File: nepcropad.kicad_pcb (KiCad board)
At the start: 2 copper layers, 99.2 x 58.7 mm, 34 parts, among them SW1 SW_Push, U1 ATmega32U4-A, Y1 16MHz

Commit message: Finished routing
I think atleast.
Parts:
- moved D1 17.5 mm to (158.0, 71.4)
- moved D2 17.5 mm to (177.0, 71.5)
- moved D3 17.5 mm to (196.1, 71.4)
- moved D4 17.5 mm to (158.0, 90.5)
- moved D5 17.5 mm to (177.0, 90.5)
- moved D6 17.5 mm to (196.1, 90.5)
- moved D7 17.5 mm to (158.0, 109.5)
- moved D8 17.5 mm to (177.0, 109.5)
- moved D9 17.5 mm to (196.1, 109.5)
- moved MX1 17.5 mm to (150.0, 71.4)
- moved MX2 17.5 mm to (169.1, 71.4)
- moved MX3 17.5 mm to (188.1, 71.4)
- moved MX4 17.5 mm to (150.0, 90.5)
- moved MX5 17.5 mm to (169.1, 90.5)
- moved MX6 17.5 mm to (188.1, 90.5)
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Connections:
- U1 pad 26: unconnected-(U1-Pad26) -> ROW0
- U1 pad 27: unconnected-(U1-Pad27) -> ROW1
- U1 pad 28: unconnected-(U1-Pad28) -> COL2
- U1 pad 29: unconnected-(U1-Pad29) -> COL1
- U1 pad 30: unconnected-(U1-Pad30) -> COL0
- U1 pad 31: unconnected-(U1-Pad31) -> ROW2
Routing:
- net COL2: track 38.1 -> 112.1 mm
- net COL1: track 38.1 -> 92.7 mm
- net ROW2: track 39.3 -> 88.3 mm
- net ROW0: track 39.2 -> 87.2 mm
- net ROW1: track 39.3 -> 81.7 mm
- net COL0: track 38.1 -> 73.3 mm
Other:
- board size 99.2 x 58.7 mm -> 116.7 x 58.7 mm

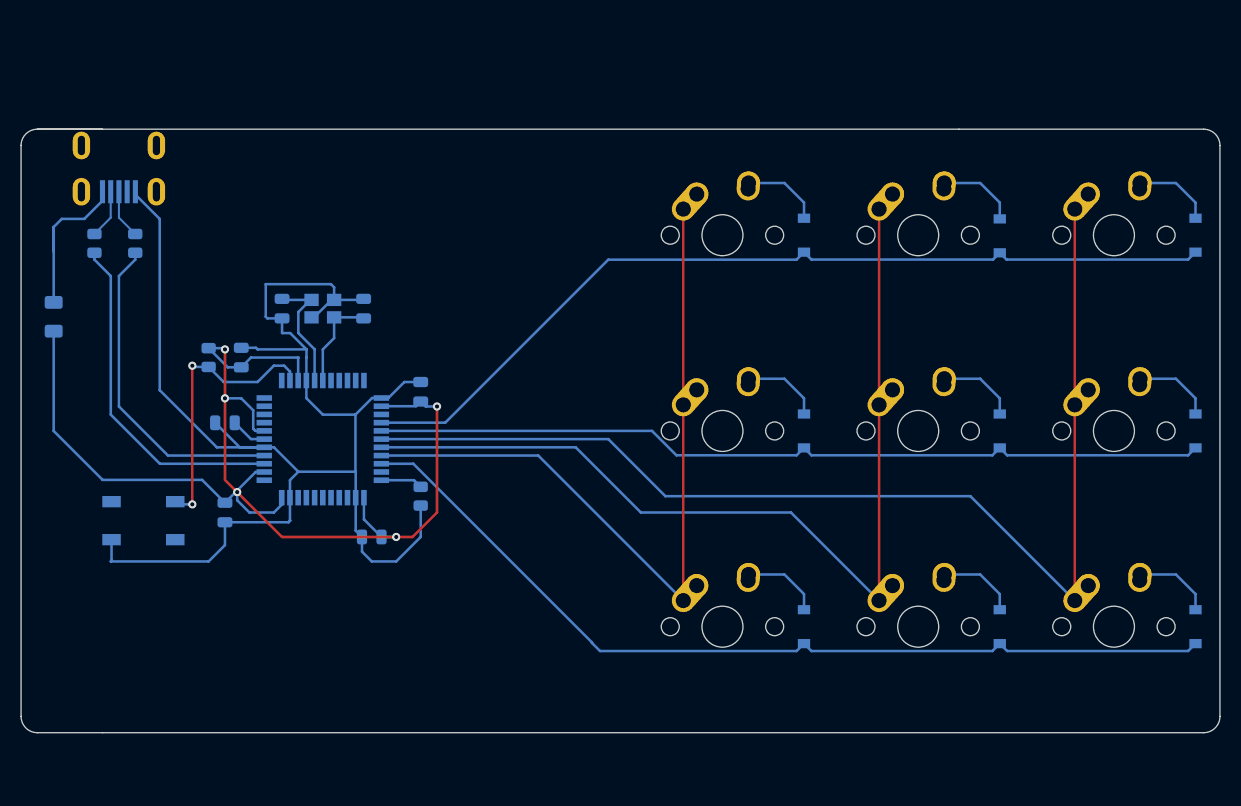
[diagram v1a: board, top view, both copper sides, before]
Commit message: Rerouted matrix
moved closer to soc for more cost efficiency probably.
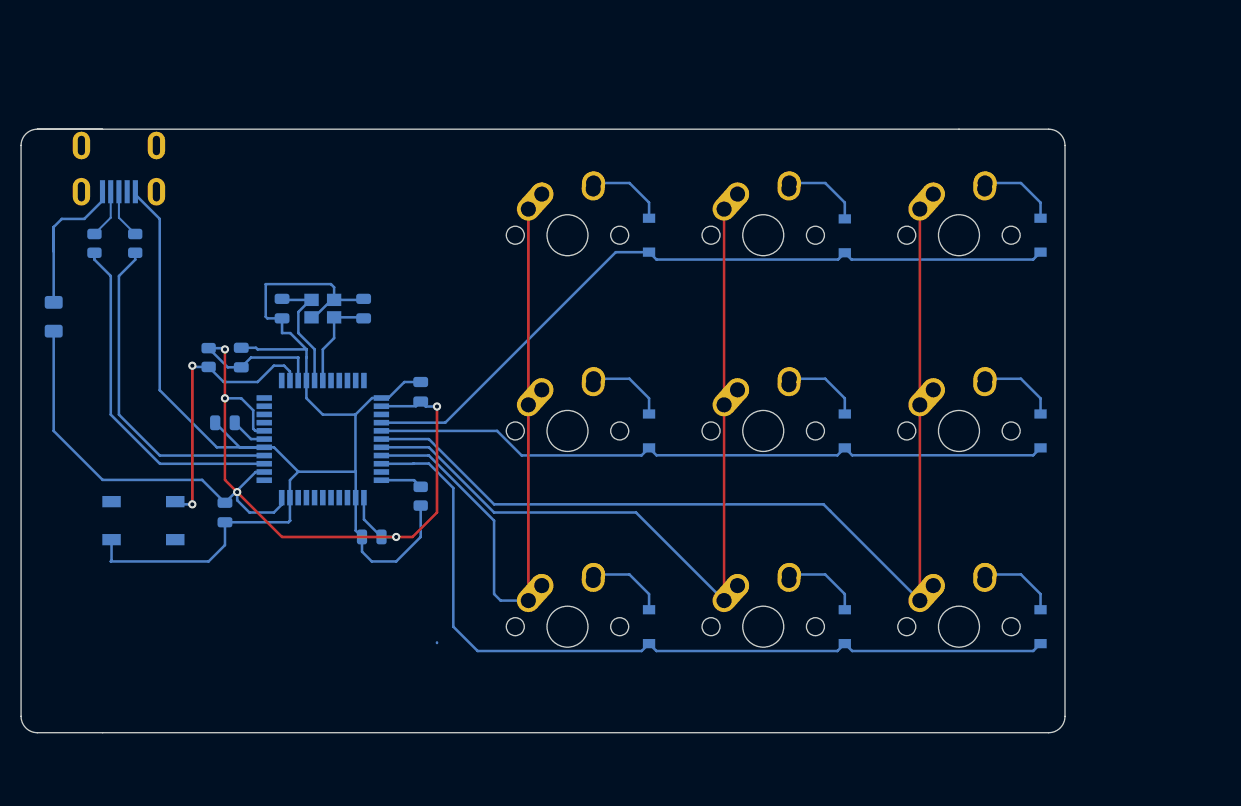
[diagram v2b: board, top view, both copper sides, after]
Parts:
- moved D1 15.1 mm to (142.9, 71.4)
- moved D3 15.1 mm to (181.0, 71.4)
- moved D4 15.1 mm to (142.9, 90.5)
- moved D6 15.1 mm to (181.0, 90.5)
- moved D7 15.1 mm to (142.9, 109.5)
- moved D9 15.1 mm to (181.0, 109.5)
- moved MX1 15.1 mm to (134.9, 71.4)
- moved MX3 15.1 mm to (173.0, 71.4)
- moved MX4 15.1 mm to (134.9, 90.5)
- moved MX6 15.1 mm to (173.0, 90.5)
- moved MX7 15.1 mm to (134.9, 109.5)
- moved MX9 15.1 mm to (173.0, 109.5)
- moved D2 15.1 mm to (161.9, 71.5)
- moved D5 15.1 mm to (161.9, 90.5)
- moved D8 15.1 mm to (161.9, 109.5)
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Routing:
- net COL2: track 112.1 -> 97.0 mm
- net COL1: track 92.7 -> 77.6 mm
- net ROW0: track 87.2 -> 72.2 mm
- net ROW1: track 81.7 -> 66.6 mm
- net COL0: track 73.3 -> 62.4 mm
- net ROW2: track 88.3 -> 81.2 mm
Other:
- board size 116.7 x 58.7 mm -> 101.6 x 58.7 mm

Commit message: minimize pcb
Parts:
- removed USB1: Molex-0548190589, random-keyboard-parts:Molex-0548190589
- added J1: USB_C_Receptacle_USB2.0, usbc:USB_C_GCT_USB4085, F.Cu at (144.8, 55.1)
- added R5: 5.1k, resistor:R_0805_2012Metric, B.Cu at (148.0, 62.9)
- added R6: 5.1k, resistor:R_0805_2012Metric, F.Cu at (137.8, 59.1)
- C4, C5, C6, C7: moved to F.Cu
- moved SW1 92.2 mm to (176.8, 59.4)
- moved F1 73.3 mm to (154.9, 57.8), turned to 0 degrees
- moved C2 71.3 mm to (178.4, 74.7), turned to 180 degrees
- moved R1 71.2 mm to (167.6, 61.0), turned to 0 degrees
- moved C7 68.3 mm to (158.8, 61.0)
- moved Y1 67.4 mm to (178.5, 77.7)
- moved C1 63.4 mm to (178.5, 81.0), turned to 0 degrees
- moved C3 61.3 mm to (159.3, 68.8), turned to 135 degrees
- moved C6 56.7 mm to (156.2, 61.0), turned to -90 degrees
- moved R3 54.6 mm to (143.5, 71.1)
- moved U1 53.9 mm to (163.5, 78.7), turned to -45 degrees
- moved R2 53.2 mm to (146.1, 71.1)
- moved C4 52.9 mm to (151.1, 61.0), turned to -90 degrees
- moved R4 43.3 mm to (163.3, 89.4), turned to 0 degrees
- moved C5 41.9 mm to (153.7, 61.0), turned to -90 degrees
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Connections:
- U1 pad 29: COL1 -> ROW2
- U1 pad 30: COL0 -> COL1
- U1 pad 31: ROW2 -> COL0
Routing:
- net COL2: track 97.0 -> 43.1 mm
- net +5V: track 119.6 -> 84.8 mm, vias 5 -> 4
- net COL0: track 62.4 -> 85.7 mm
- net Net-(R2-Pad2): track 32.2 -> 13.9 mm
- net Net-(R3-Pad2): track 33.3 -> 16.1 mm
- net GND: track 147.2 -> 132.9 mm, vias 0 -> 3
- net Net-(C1-Pad2): track 9.52 -> 22.0 mm
- net ROW1: track 66.6 -> 54.4 mm
- net ROW2: track 81.2 -> 71.2 mm, vias 0 -> 2
- net Net-(J1-PadB5): track 0.00 -> 7.41 mm
- net COL1: track 77.6 -> 70.5 mm
- net D+: track 4.77 -> 11.1 mm
- net D-: track 4.77 -> 11.1 mm
- net Net-(C3-Pad1): track 3.53 -> 7.69 mm
- net Net-(D1-Pad2): track 7.71 -> 3.96 mm
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- added copper zone on F.Cu, net GND
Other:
- board size 101.6 x 58.7 mm -> 58.7 x 65.2 mm

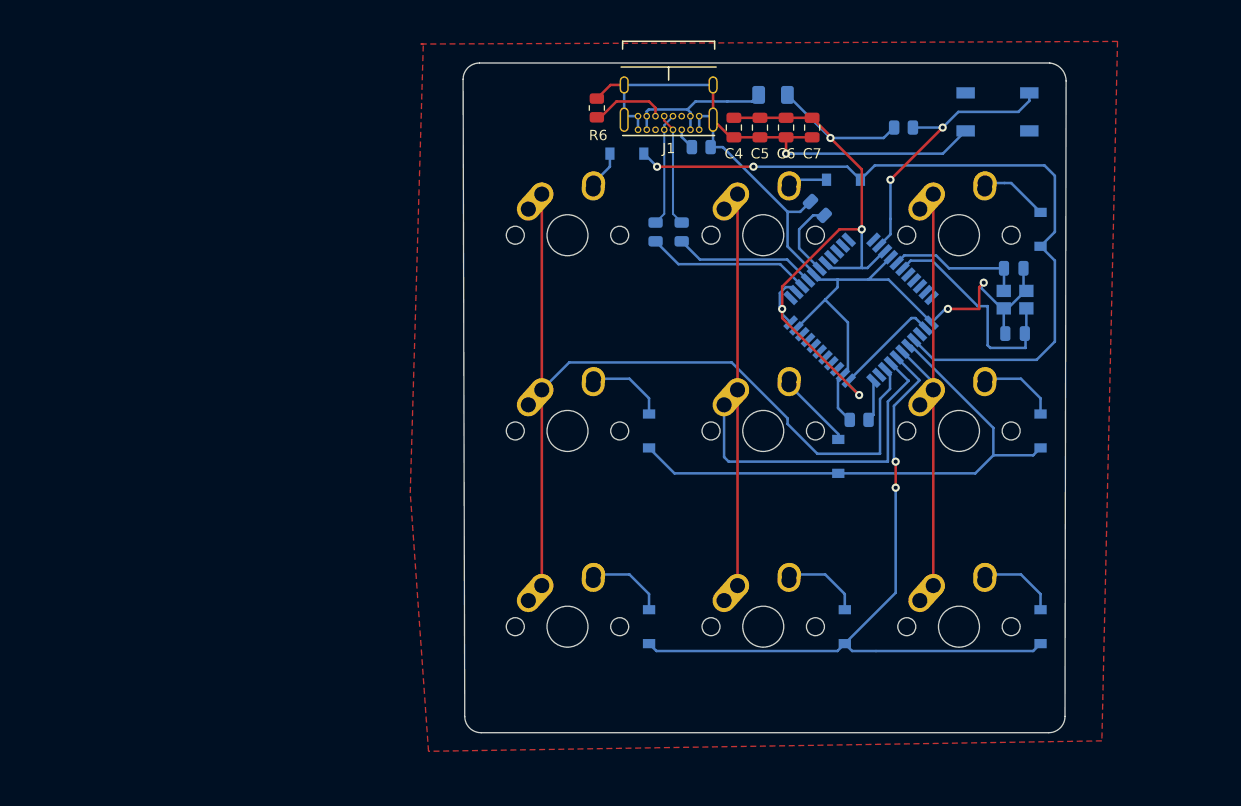
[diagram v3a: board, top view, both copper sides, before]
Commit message: move SMC's to same side to cut costs
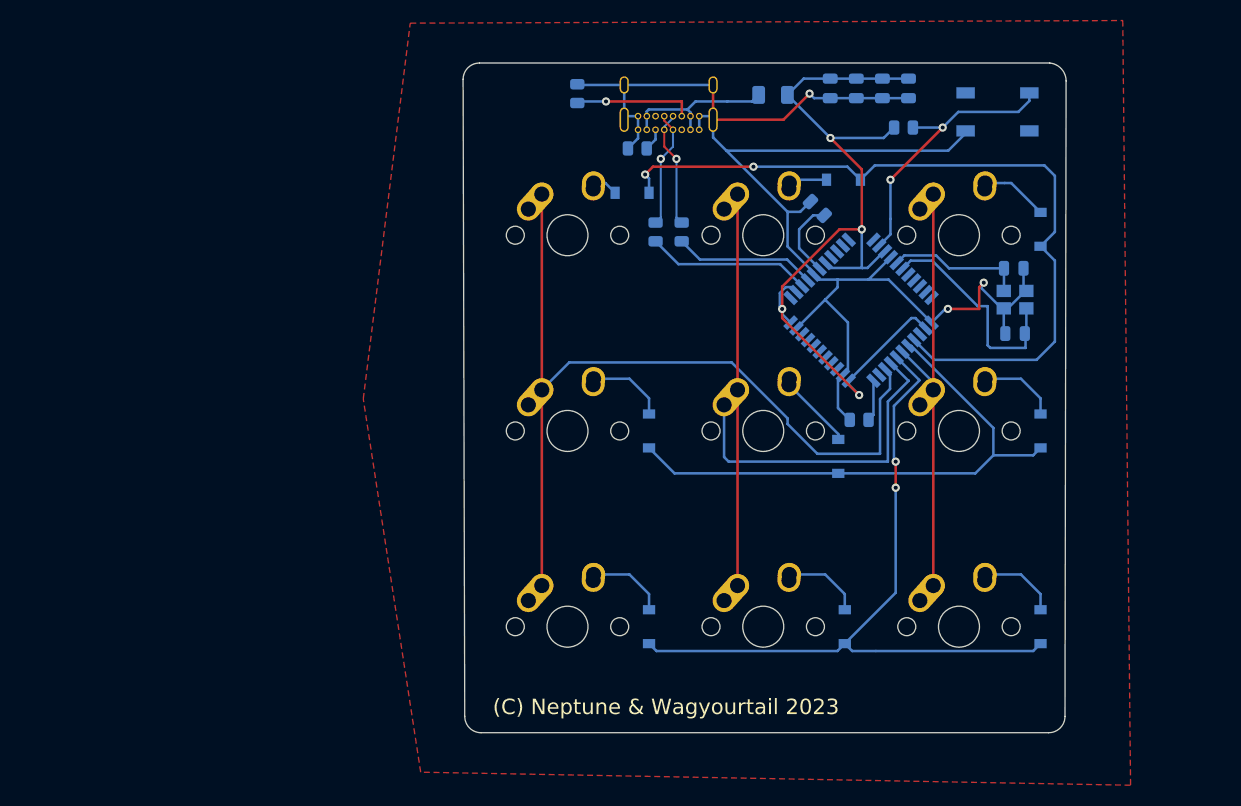
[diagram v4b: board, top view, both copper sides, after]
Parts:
- C4, C5, C6, C7, J1, R6: moved to B.Cu
- moved C4 17.4 mm to (168.1, 57.1)
- moved C5 12.5 mm to (165.6, 57.1)
- moved C6 7.83 mm to (163.0, 57.1)
- moved R5 6.22 mm to (141.7, 63.0), turned to 180 degrees
- moved C7 4.20 mm to (160.5, 57.1)
- moved D1 3.84 mm to (141.2, 67.3)
- moved R6 2.36 mm to (135.9, 57.7)
- turned J1 to 0 degrees
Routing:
- net GND: track 132.9 -> 150.1 mm
- net Net-(J1-PadB5): track 7.41 -> 11.9 mm, vias 0 -> 1
- net +5V: track 84.8 -> 87.1 mm
- net ROW0: track 74.6 -> 76.2 mm
- net Net-(D1-Pad2): track 3.96 -> 2.49 mm
- net D-: track 11.1 -> 11.4 mm, vias 0 -> 1
- net D+: track 11.1 -> 11.4 mm, vias 0 -> 1
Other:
- board text added: "(C) Neptune & Wagyourtail 2023"

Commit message: cleanup
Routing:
- net COL0: track 85.7 -> 85.0 mm
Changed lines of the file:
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@@
   (segment (start 160.011508 77.715508) (end 157.21925 80.507767) (width 0.25) (layer "B.Cu") (net 1))
   (segment (start 179.319 76.581) (end 179.596 76.858) (width 0.25) (layer "B.Cu") (net 1))
-  (segment (start 168.12569 58.1) (end 168.43569 58.1) (width 0.25) (layer "B.Cu") (net 1))
   (segment (start 141.805 61.175) (end 141.805 62.0065) (width 0.25) (layer "B.Cu") (net 1))
   (segment (start 161.222725 75.759275) (end 164.230483 75.759275) (width 0.25) (layer "B.Cu") (net 1))
@@
   (segment (start 158.840249 69.505751) (end 159.929751 69.505751) (width 0.25) (layer "B.Cu") (net 4))
   (segment (start 160.528 61.976) (end 163.576 65.024) (width 0.25) (layer "F.Cu") (net 5))
-  (segment (start 160.528 61.976) (end 160.528 61.788) (width 0.25) (layer "F.Cu") (net 5))
   (segment (start 163.576 70.866) (end 161.406769 70.866) (width 0.25) (layer "F.Cu") (net 5))
   (segment (start 155.829 79.502) (end 155.829 78.613) (width 0.25) (layer "F.Cu") (net 5))
@@
   (segment (start 165.354 92.71) (end 159.258 92.71) (width 0.25) (layer "B.Cu") (net 19))
   (segment (start 156.356401 89.262861) (end 150.91354 83.82) (width 0.25) (layer "B.Cu") (net 19))
-  (segment (start 165.845952 84.467565) (end 166.37 84.991613) (width 0.25) (layer "B.Cu") (net 19))
   (segment (start 165.354 87.376) (end 165.354 92.71) (width 0.25) (layer "B.Cu") (net 19))
   (segment (start 166.330051 84.951664) (end 166.330051 86.399949) (width 0.25) (layer "B.Cu") (net 19))
@@
   (segment (start 166.411638 83.90188) (end 168.107758 85.598) (width 0.25) (layer "B.Cu") (net 20))
   (segment (start 166.116 87.63) (end 166.116 93.472) (width 0.25) (layer "B.Cu") (net 20))
-  (segment (start 168.107758 85.598) (end 168.148 85.598) (width 0.25) (layer "B.Cu") (net 20))
   (segment (start 150.1775 93.0275) (end 150.1775 87.9475) (width 0.25) (layer "B.Cu") (net 20))
   (segment (start 168.148 85.598) (end 166.116 87.63) (width 0.25) (layer "B.Cu") (net 20))
@@
   (segment (start 146.06 58.43) (end 146.05 58.42) (width 0.25) (layer "F.Cu") (net 49))
   (via (at 138.684 58.42) (size 0.8) (drill 0.4) (layers "F.Cu" "B.Cu") (net 49))
-  (segment (start 138.5335 58.5705) (end 138.684 58.42) (width 0.25) (layer "B.Cu") (net 49))
   (segment (start 136.0405 58.42) (end 135.89 58.5705) (width 0.25) (layer "B.Cu") (net 49))
   (segment (start 138.684 58.42) (end 136.0405 58.42) (width 0.25) (layer "B.Cu") (net 49))

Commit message: move some caps and the timer
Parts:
- moved C4 30.7 mm to (147.6, 80.0)
- moved C5 27.9 mm to (149.6, 80.0)
- moved C6 25.5 mm to (151.6, 80.0)
- moved C7 23.9 mm to (153.7, 80.0)
- moved Y1 3.57 mm to (175.3, 76.2), turned to 135 degrees
- moved C1 2.70 mm to (177.5, 78.5), turned to -135 degrees
- moved C2 0.96 mm to (177.5, 74.2), turned to 135 degrees
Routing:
- net Net-(C1-Pad2): track 22.0 -> 11.9 mm
- net GND: track 149.8 -> 141.1 mm, vias 3 -> 0
- net +5V: track 86.9 -> 82.9 mm
- net Net-(C2-Pad2): track 13.5 -> 11.3 mm

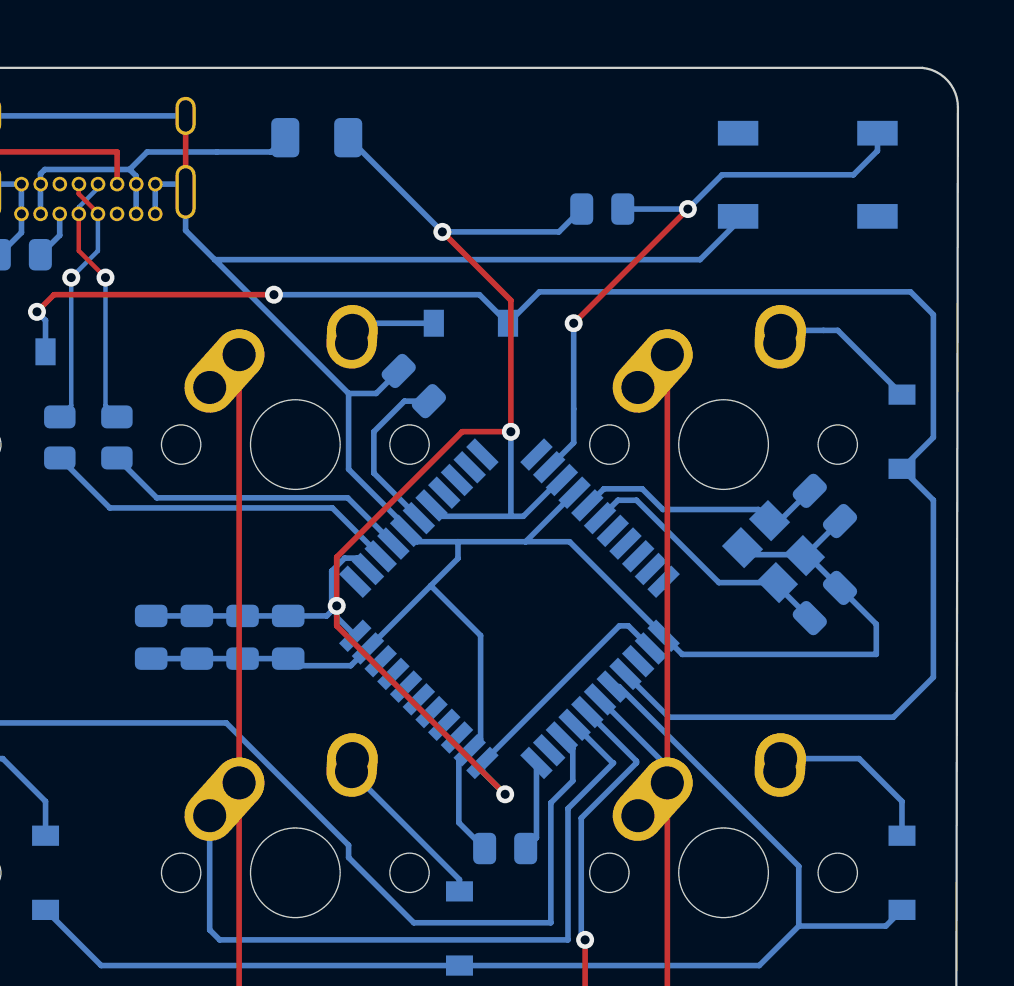
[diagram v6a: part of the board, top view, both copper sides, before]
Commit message: update cap positions
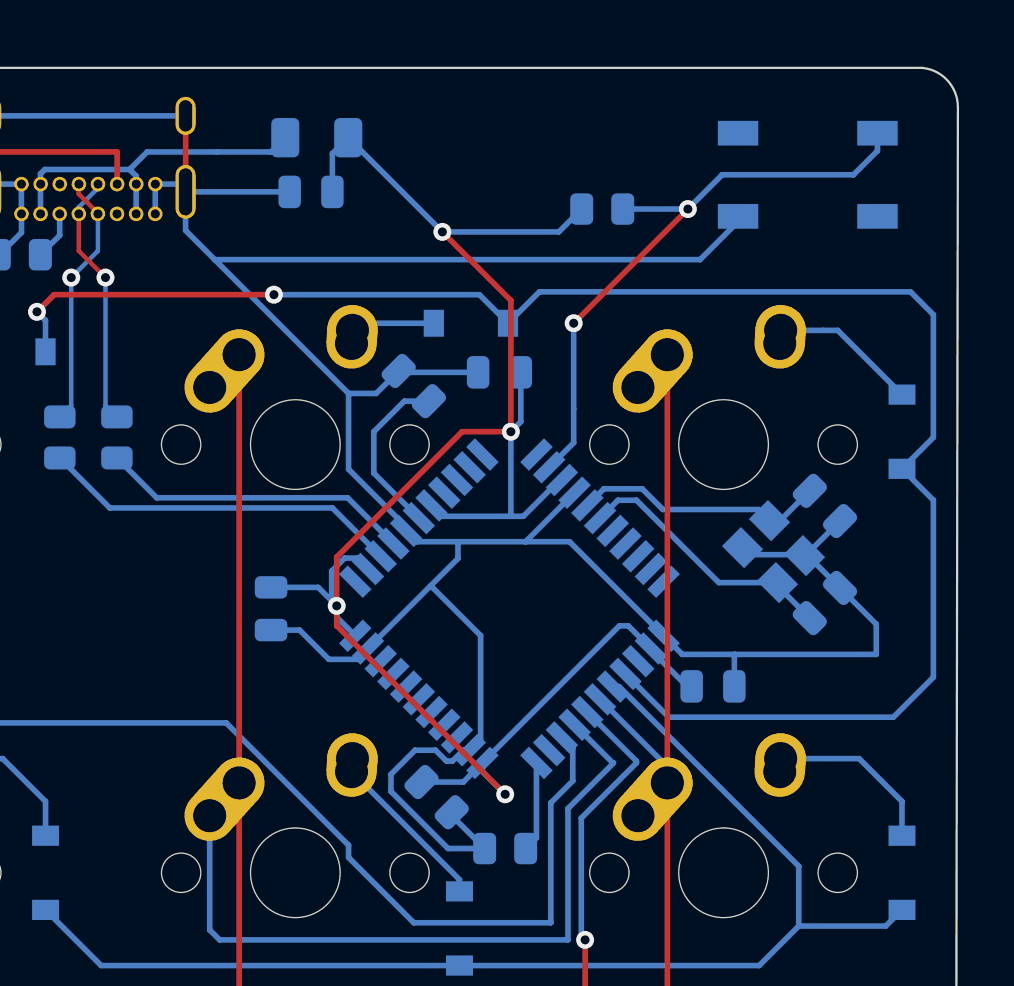
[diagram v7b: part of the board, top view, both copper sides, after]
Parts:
- added C8: 0.1uF, Capacitor_SMD:C_0805_2012Metric, B.Cu at (163.1, 68.2)
- moved C4 25.1 mm to (172.6, 82.2), turned to 0 degrees
- moved C7 19.8 mm to (154.7, 60.2), turned to 180 degrees
- moved C5 12.8 mm to (160.3, 87.1), turned to -45 degrees
- moved C6 1.80 mm to (152.9, 78.7)
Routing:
- net GND: track 141.1 -> 153.1 mm
- net +5V: track 82.9 -> 88.5 mm
